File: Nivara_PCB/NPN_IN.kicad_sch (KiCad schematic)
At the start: 8 parts, among them U4 LTV-357T, U5 LTV-357T

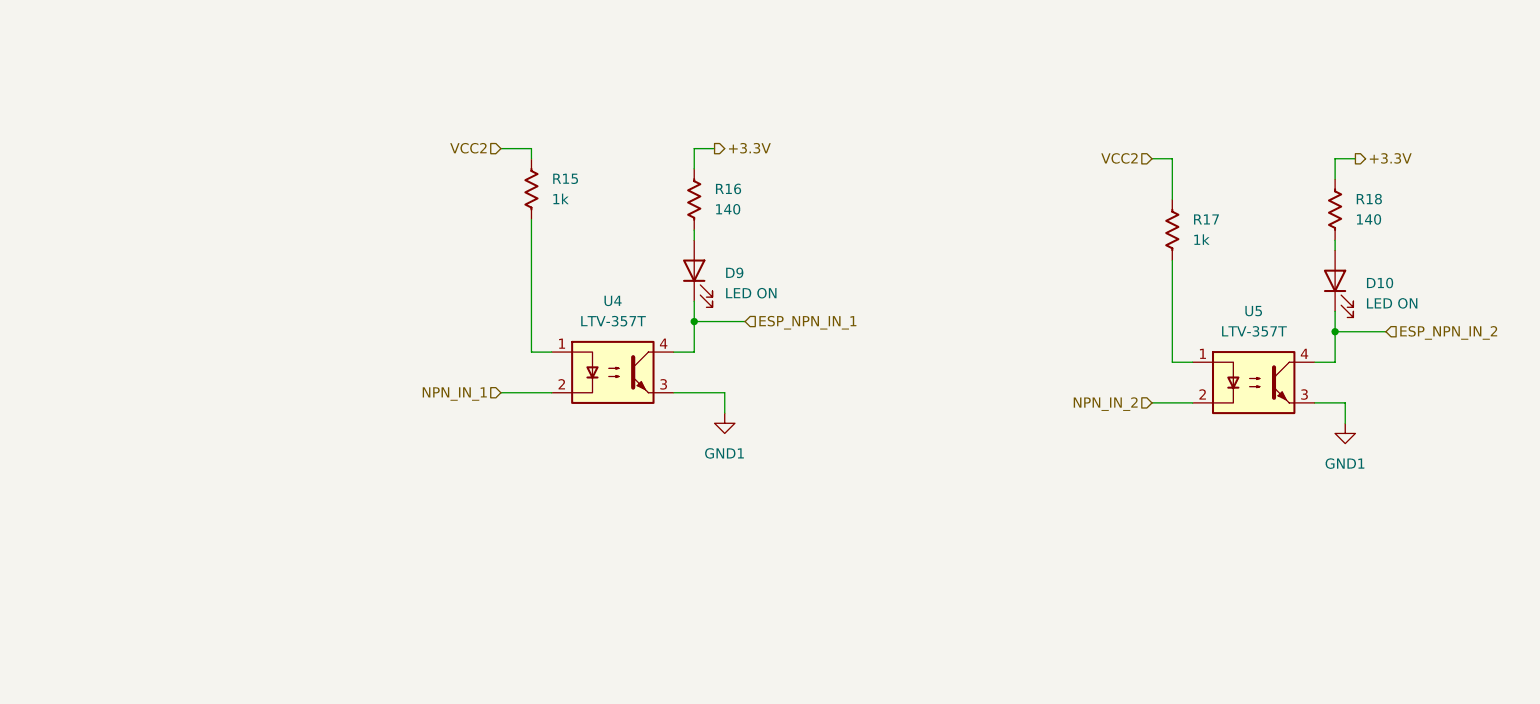
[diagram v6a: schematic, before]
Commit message: Cambios realizados en el PCB y el esquema de Nivara_PCB.
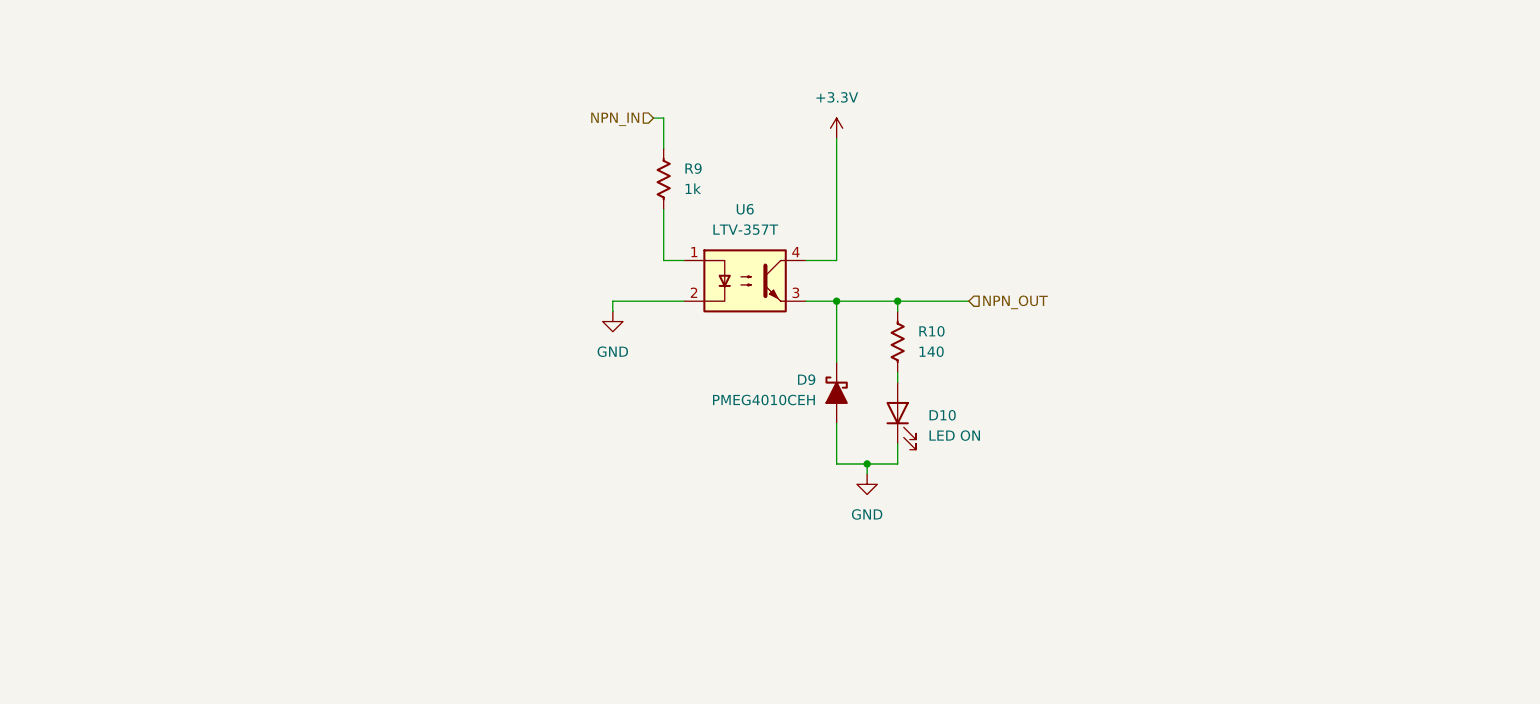
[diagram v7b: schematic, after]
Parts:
- removed D9: LED ON, LED_SMD:LED_0603_1608Metric, symbol Device:LED
- removed R15, R17: 1k, PCM_Resistor_SMD_AKL:R_0603_1608Metric, symbol PCM_Resistor_US_AKL:R_0603
- removed R16, R18: 140, PCM_Resistor_SMD_AKL:R_0603_1608Metric, symbol PCM_Resistor_US_AKL:R_0603
- removed U4, U5: LTV-357T, Package_SO:SO-4_4.4x3.6mm_P2.54mm, symbol Isolator:LTV-357T
- added D9: PMEG4010CEH, PCM_Diode_SMD_AKL:D_SOD-123F, symbol PCM_Diode_Schottky_AKL:PMEG4010CEH
- added R10: 140, PCM_Resistor_SMD_AKL:R_0603_1608Metric, symbol PCM_Resistor_US_AKL:R_0603
- added R9: 1k, PCM_Resistor_SMD_AKL:R_0603_1608Metric, symbol PCM_Resistor_US_AKL:R_0603
- added U6: LTV-357T, Package_SO:SO-4_4.4x3.6mm_P2.54mm, symbol Isolator:LTV-357T
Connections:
- net +3.3V: now also U6.4
- net at D10.2 (A): now also R10.2
- net ESP_NPN_IN_2 renamed GND
- net GND: now also D9.2 (A), U6.2
- new net: R9.2, U6.1
- new net NPN_IN: R9.1
- new net NPN_OUT: D9.1 (K), R10.1, U6.3

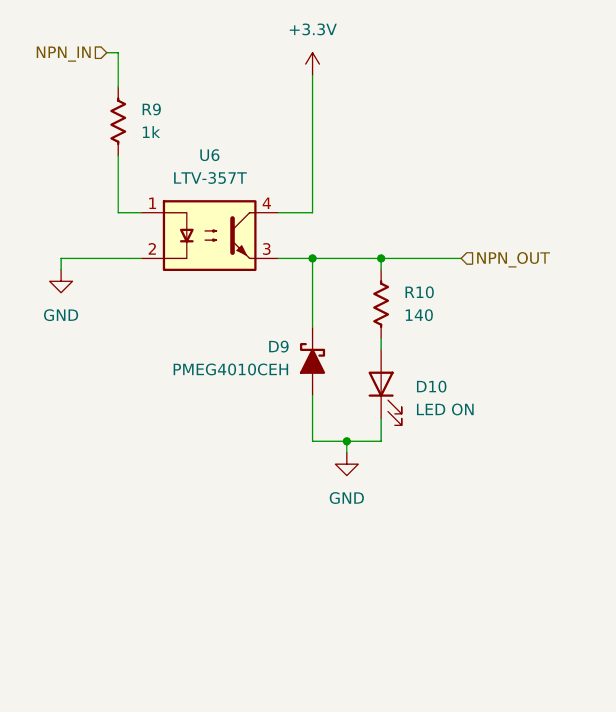
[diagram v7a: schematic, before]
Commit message: Cambios realizados en los archivos de Nivara_PCB.
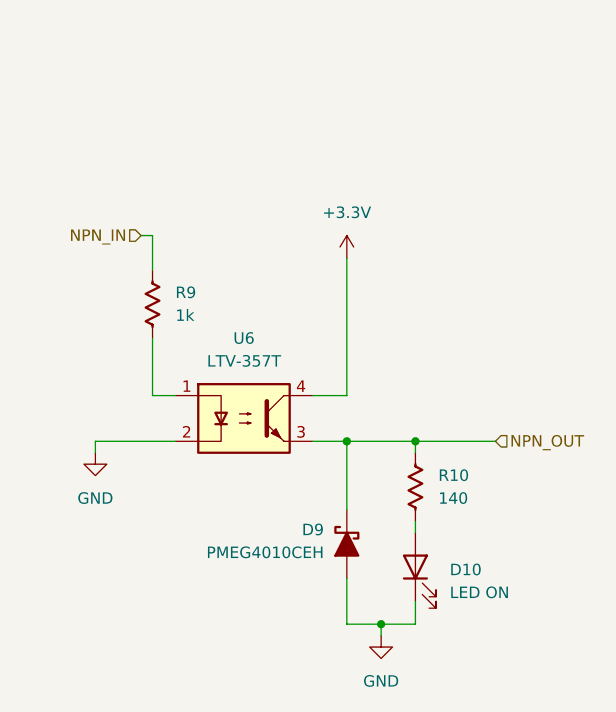
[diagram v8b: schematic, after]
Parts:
- D10: symbol Device:LED -> EasyEDA:LED
- D9: symbol PCM_Diode_Schottky_AKL:PMEG4010CEH -> EasyEDA:PMEG4010CEH
- R10, R9: symbol PCM_Resistor_US_AKL:R_0603 -> EasyEDA:R_0603
- U6: symbol Isolator:LTV-357T -> EasyEDA:LTV-357T
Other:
- moved on the sheet: D10, D9, R10, R9, U6
